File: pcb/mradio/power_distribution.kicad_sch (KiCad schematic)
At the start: 2 parts, among them U3 TPS54560BDDA, U4 TXB0108PW

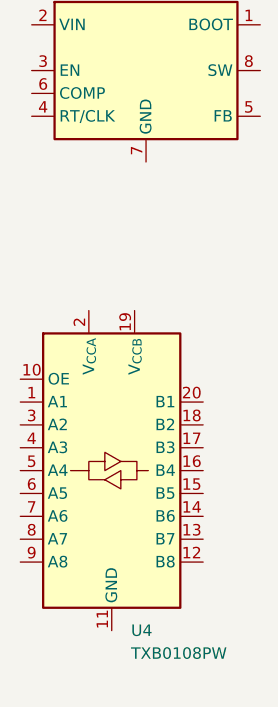
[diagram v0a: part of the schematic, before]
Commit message: Add ground to power schematic
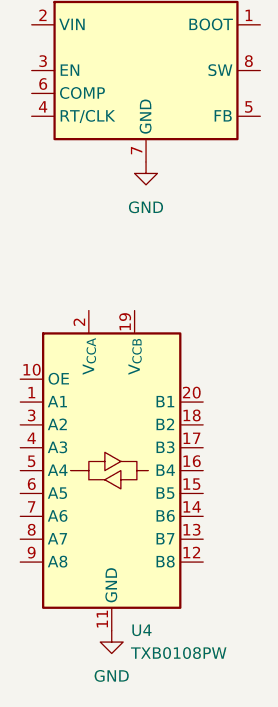
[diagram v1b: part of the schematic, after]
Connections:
- net GND: now reaches U4.11 (GND)
- net GND: now also U3.7 (GND), U3.9 (GND)
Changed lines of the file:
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@@
 	(paper "A4")
+	(symbol
+		(lib_id "power:GND")
+		(at 76.2 73.66 0)
+		(unit 1)
+		(body_style 1)
+		(exclude_from_sim no)
+		(in_bom yes)
+		(on_board yes)
+		(in_pos_files yes)
+		(dnp no)
+		(fields_autoplaced yes)
+		(property "Reference" "#PWR01"
+			(at 76.2 80.01 0)
+			(hide yes)
+			(show_name no)
+			(do_not_autoplace no)
+			(effects
+				(font
+					(size 1.27 1.27)
+				)
+			)
+		)
+		(property "Value" "GND"
+			(at 76.2 78.74 0)
+			(show_name no)
+			(do_not_autoplace no)
+			(effects
+				(font
+					(size 1.27 1.27)
+				)
+			)
+		)
+		(property "Footprint" ""
+			(at 76.2 73.66 0)
+			(hide yes)
+			(show_name no)
+			(do_not_autoplace no)
+			(effects
+				(font
+					(size 1.27 1.27)
+				)
+			)
+		)
+		(property "Datasheet" ""
+			(at 76.2 73.66 0)
+			(hide yes)
+			(show_name no)
+			(do_not_autoplace no)
+			(effects
+				(font
+					(size 1.27 1.27)
+				)
+			)
+		)
+		(property "Description" "Power symbol creates a global label with name \"GND\" , ground"
+			(at 76.2 73.66 0)
+			(hide yes)
+			(show_name no)
+			(do_not_autoplace no)
+			(effects
+				(font
+					(size 1.27 1.27)
+				)
+			)
+		)
+		(pin "1"
+		)
+		(instances
+			(project "mradio"
+				(path "/2cc0edad-946a-464e-a48b-49648a6334ed"
+					(reference "#PWR01")
+					(unit 1)
+				)
+			)
+		)
+	)
 	(symbol
 		(lib_id "Logic_LevelTranslator:TXB0108PW")
@@
 					(unit 1)
 				)
+			)
+		)
+	)
+	(symbol
+		(lib_id "power:GND")
+		(at 72.39 125.73 0)
+		(unit 1)
+		(body_style 1)
+		(exclude_from_sim no)
+		(in_bom yes)
+		(on_board yes)
+		(in_pos_files yes)
+		(dnp no)
+		(fields_autoplaced yes)
+		(property "Reference" "#PWR02"
+			(at 72.39 132.08 0)
+			(hide yes)
+			(show_name no)
+			(do_not_autoplace no)
+			(effects
+				(font
+					(size 1.27 1.27)
+				)
+			)
+		)
+		(property "Value" "GND"
+			(at 72.39 130.81 0)
+			(show_name no)
+			(do_not_autoplace no)
+			(effects
+				(font
+					(size 1.27 1.27)
+				)
+			)
+		)
+		(property "Footprint" ""
+			(at 72.39 125.73 0)
+			(hide yes)
+			(show_name no)
+			(do_not_autoplace no)
+			(effects
+				(font
+					(size 1.27 1.27)
+				)
+			)
+		)
+		(property "Datasheet" ""
+			(at 72.39 125.73 0)
+			(hide yes)
+			(show_name no)
+			(do_not_autoplace no)
+			(effects
+				(font
+					(size 1.27 1.27)
+				)
+			)
+		)
+		(property "Description" "Power symbol creates a global label with name \"GND\" , ground"
+			(at 72.39 125.73 0)
+			(hide yes)
+			(show_name no)
+			(do_not_autoplace no)
+			(effects
+				(font
+					(size 1.27 1.27)
+				)
+			)
+		)
+		(pin "1"
+		)
+		(instances
+			(project "mradio"
+				(path "/2cc0edad-946a-464e-a48b-49648a6334ed"
+					(reference "#PWR02")
+					(unit 1)
+				)

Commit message: Input caps
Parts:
- added C10: 100uF, symbol Device:C_Polarized_US
- added C2, C3, C4: 2.2uF, symbol Device:C
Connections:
- net GND: now also C10.2, C2.2, C3.2, C4.2
- net +12V: now reaches U3.2 (VIN)
- net +12V: now also C10.1, C2.1, C3.1, C4.1
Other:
- moved on the sheet: U3, U4

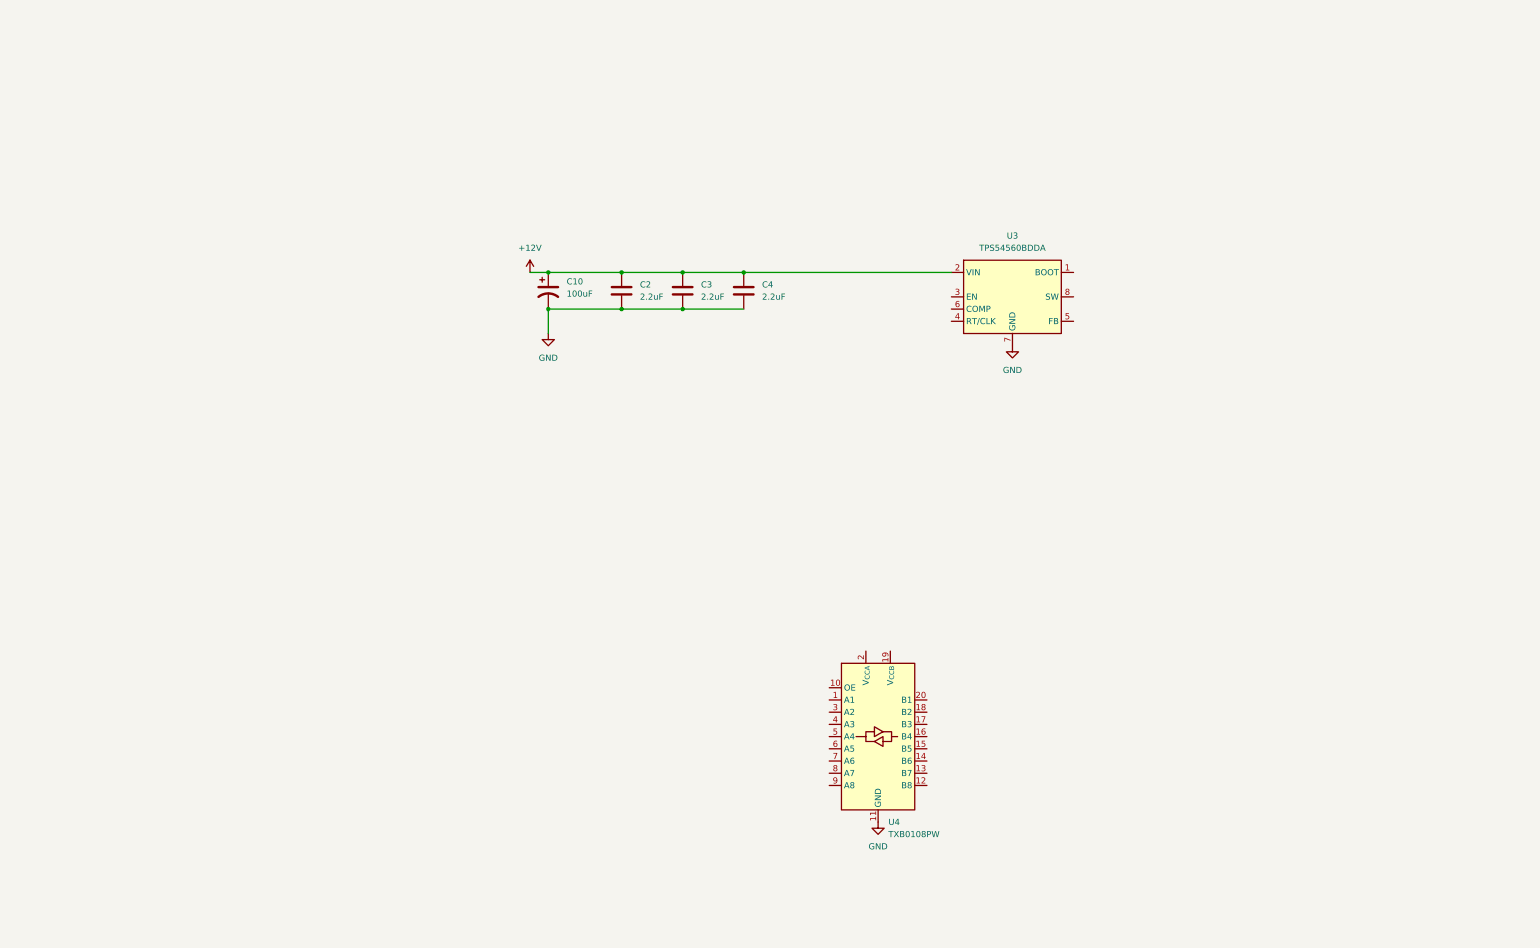
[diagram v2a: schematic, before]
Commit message: Finished buck
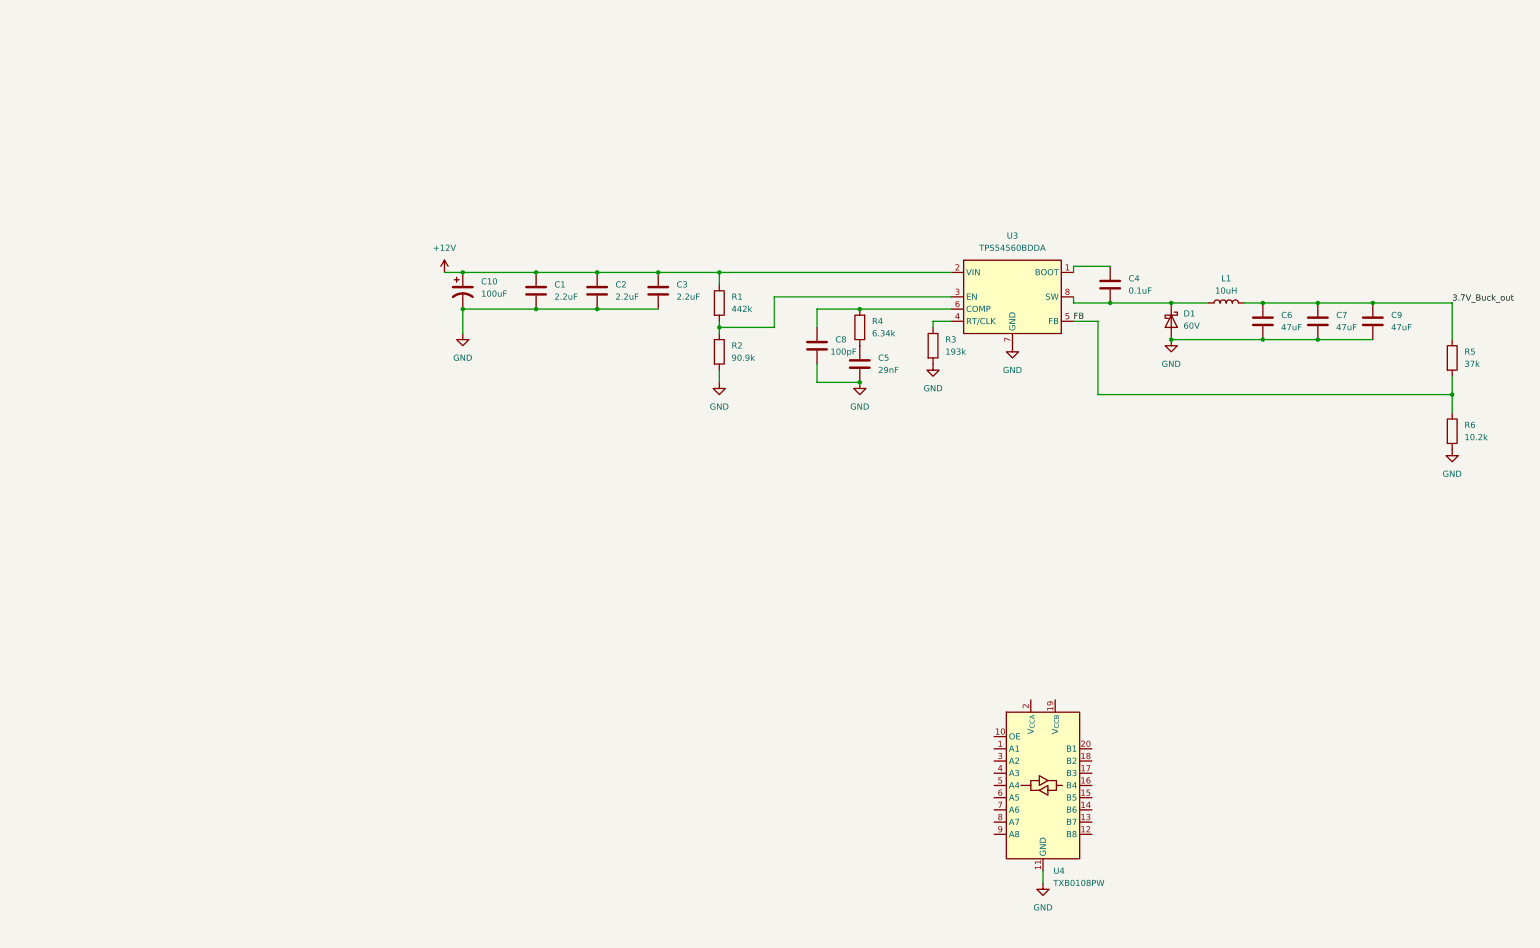
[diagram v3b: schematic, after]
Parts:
- added C4: 0.1uF, symbol Device:C
- added C5: 29nF, symbol Device:C
- added C6, C7, C9: 47uF, symbol Device:C
- added C8: 100pF, symbol Device:C
- added D1: 60V, symbol Device:D_Schottky
- added L1: 10uH, symbol Device:L
- added R1: 442k, symbol Device:R
- added R2: 90.9k, symbol Device:R
- added R3: 193k, symbol Device:R
- added R4: 6.34k, symbol Device:R
- added R5: 37k, symbol Device:R
- added R6: 10.2k, symbol Device:R
- renumbered C2 to C1, C3 to C2, C4 to C3
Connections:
- net +12V: now also R1.1
- net GND: now also C5.2, C6.2, C7.2, C8.2, C9.2, D1.2 (A), R2.2, R3.2, R6.2
- net at U3.1 (BOOT): now also C4.1
- net at U3.3 (EN): now also R1.2, R2.1
- net at U3.4 (RT/CLK): now also R3.1
- net FB: now reaches U3.5 (FB)
- net FB: now also R5.2, R6.1
- net at U3.6 (COMP): now also C8.1, R4.2
- net at U3.8 (SW): now also C4.2, D1.1 (K), L1.1
- new net: C5.1, R4.1
- new net 3.7V_Buck_out: C6.1, C7.1, C9.1, L1.2, R5.1
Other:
- moved on the sheet: C1, C10, C2, C3, U4

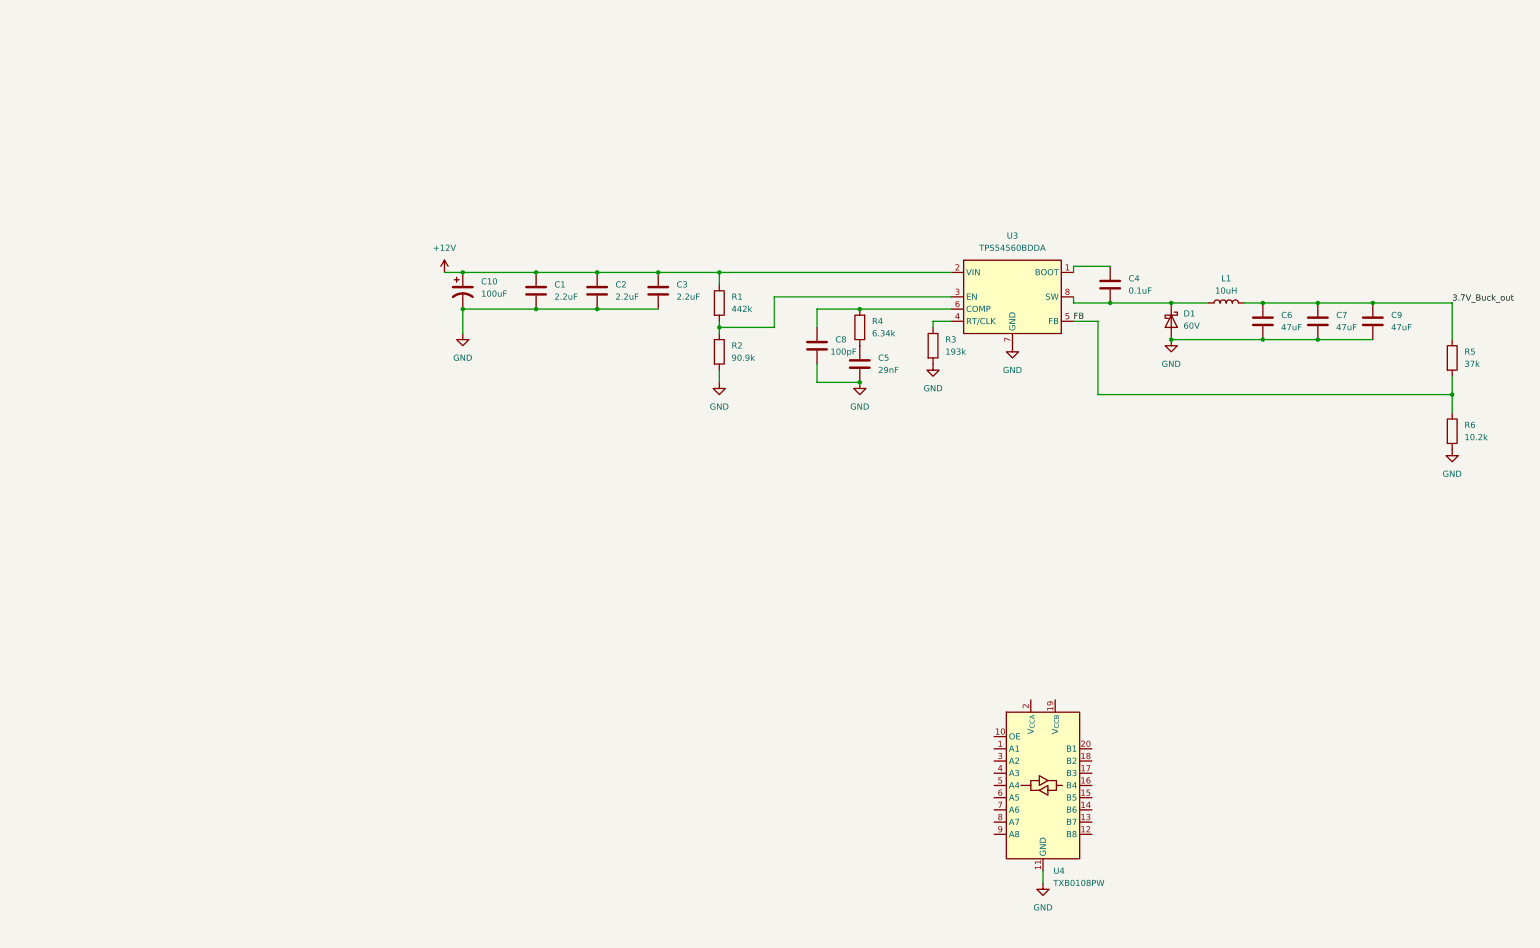
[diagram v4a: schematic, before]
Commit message: Added 5.3V Buck
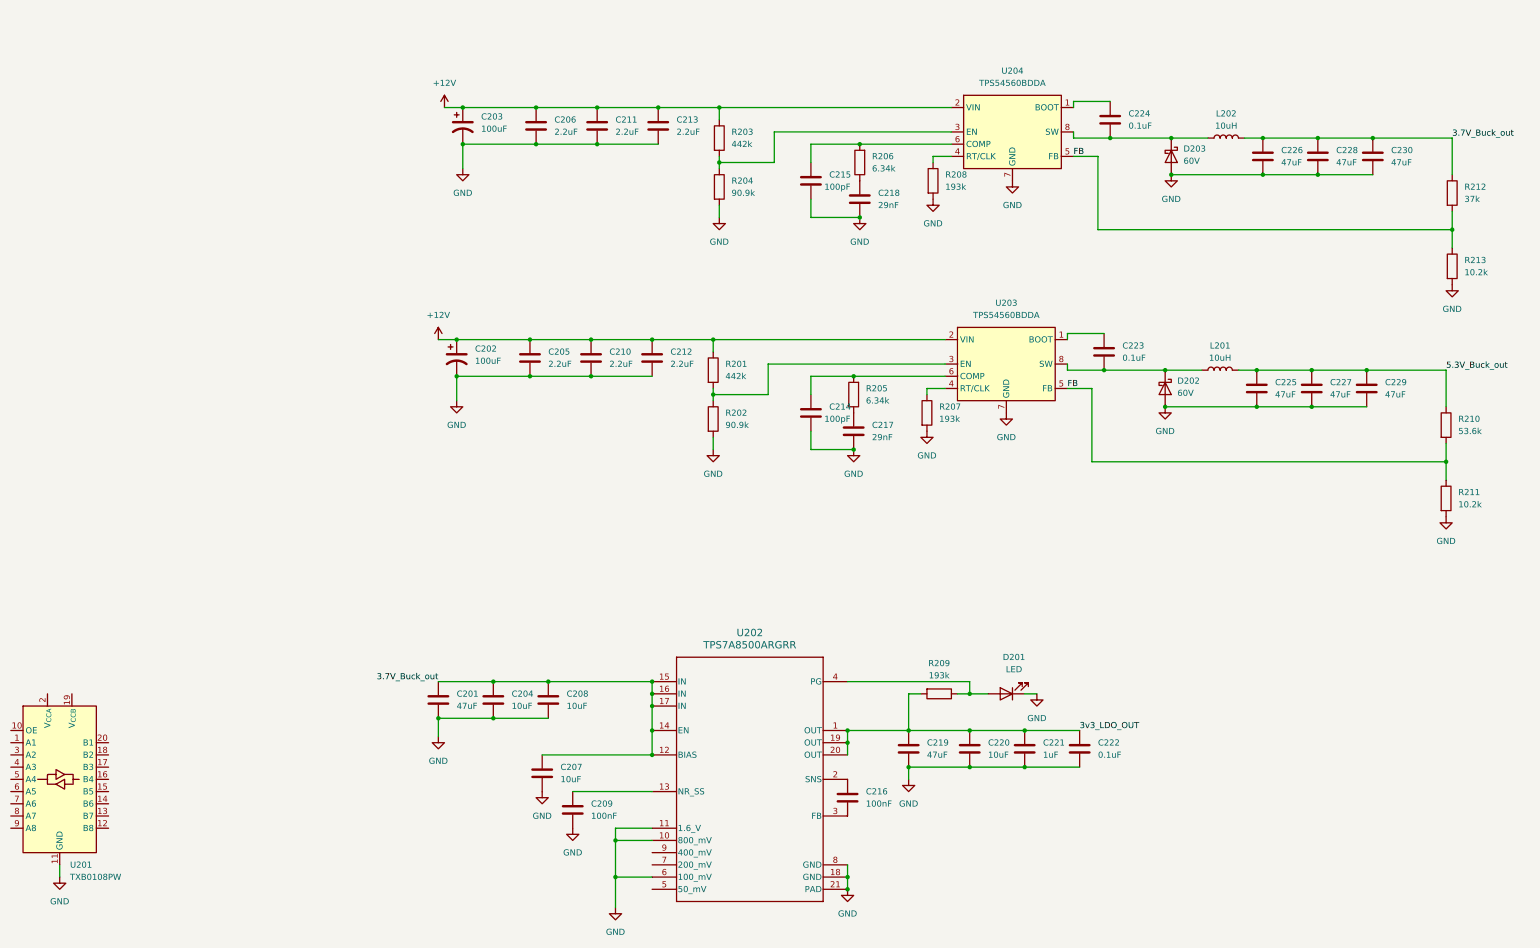
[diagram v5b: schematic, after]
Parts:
- added C201: 47uF, RGR0020A, symbol Device:C
- added C202: 100uF, symbol Device:C_Polarized_US
- added C204, C207, C208: 10uF, RGR0020A, symbol Device:C
- added C205, C210, C212: 2.2uF, symbol Device:C
- added C209, C216: 100nF, symbol Device:C
- added C214: 100pF, symbol Device:C
- added C217: 29nF, symbol Device:C
- added C219, C225, C227, C229: 47uF, symbol Device:C
- added C220: 10uF, symbol Device:C
- added C221: 1uF, symbol Device:C
- added C222, C223: 0.1uF, symbol Device:C
- added D201: LED, symbol Device:LED
- added D202: 60V, symbol Device:D_Schottky
- added L201: 10uH, symbol Device:L
- added R201: 442k, symbol Device:R
- added R202: 90.9k, symbol Device:R
- added R205: 6.34k, symbol Device:R
- added R207, R209: 193k, symbol Device:R
- added R210: 53.6k, symbol Device:R
- added R211: 10.2k, symbol Device:R
- added U202: TPS7A8500ARGRR, RGR0020A, symbol symbols:TPS7A8500ARGRR
- added U203: TPS54560BDDA, Package_SO:Texas_R-PDSO-G8_EP2.95x4.9mm_Mask2.4x3.1mm_ThermalVias, symbol Regulator_Switching:TPS54560BDDA
- renumbered C10 to C203, C1 to C206, C2 to C211, C3 to C213, C8 to C215, C5 to C218, C4 to C224, C6 to C226, C7 to C228, C9 to C230, D1 to D203, L1 to L202, R1 to R203, R2 to R204, R4 to R206, R3 to R208, R5 to R212, R6 to R213, U4 to U201, U3 to U204
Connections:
- net +12V: now also C202.1, C205.1, C210.1, C212.1, R201.1, U203.2 (VIN)
- net 3.7V_Buck_out: now also C201.1, C204.1, C207.1, C208.1, U202.12 (BIAS), U202.14 (EN), U202.15 (IN), U202.16 (IN), U202.17 (IN)
- net FB: now also R210.2, R211.1, U203.5 (FB)
- net GND: now also C201.2, C202.2, C204.2, C205.2, C207.2, C208.2, C209.2, C210.2, C212.2, C214.2, C217.2, C219.2, C220.2, C221.2, C222.2, C225.2, C227.2, C229.2, D201.1 (K), D202.2 (A), R202.2, R207.2, R211.2, U202.10 (800_mV), U202.11 (1.6_V), U202.18 (GND), U202.21 (PAD), U202.6 (100_mV), U202.8 (GND), U203.7 (GND), U203.9 (GND)
- new net: C223.1, U203.1 (BOOT)
- new net: C223.2, D202.1 (K), L201.1, U203.8 (SW)
- new net: C216.1, U202.2 (SNS)
- new net: C216.2, U202.3 (FB)
- new net: C209.1, U202.13 (NR_SS)
- new net: R201.2, R202.1, U203.3 (EN)
- new net: R207.1, U203.4 (RT/CLK)
- new net: C214.1, R205.2, U203.6 (COMP)
- new net: D201.2 (A), R209.1, U202.4 (PG)
- new net: C217.1, R205.1
- new net 3v3_LDO_OUT: C219.1, C220.1, C221.1, C222.1, R209.2, U202.1 (OUT), U202.19 (OUT), U202.20 (OUT)
- new net 5.3V_Buck_out: C225.1, C227.1, C229.1, L201.2, R210.1
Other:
- moved on the sheet: C203, C206, C211, C213, C215, C218, C224, C226, C228, C230, D203, L202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
